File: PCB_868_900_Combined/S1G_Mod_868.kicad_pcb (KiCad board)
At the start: 4 copper layers, 60 x 27 mm, 82 parts, among them J2 20021121-00010C4LF, J5 0475890001-MicroUSBPort, P1 61301621121, Q1 DMG2307L-7, SW1 CUS-12TB, SW2 B3U-1000P, T1 0732511150, U1 AP7361-33FGE-7, U2 ADF7023BCPZ, U3 STM32L052C8T6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

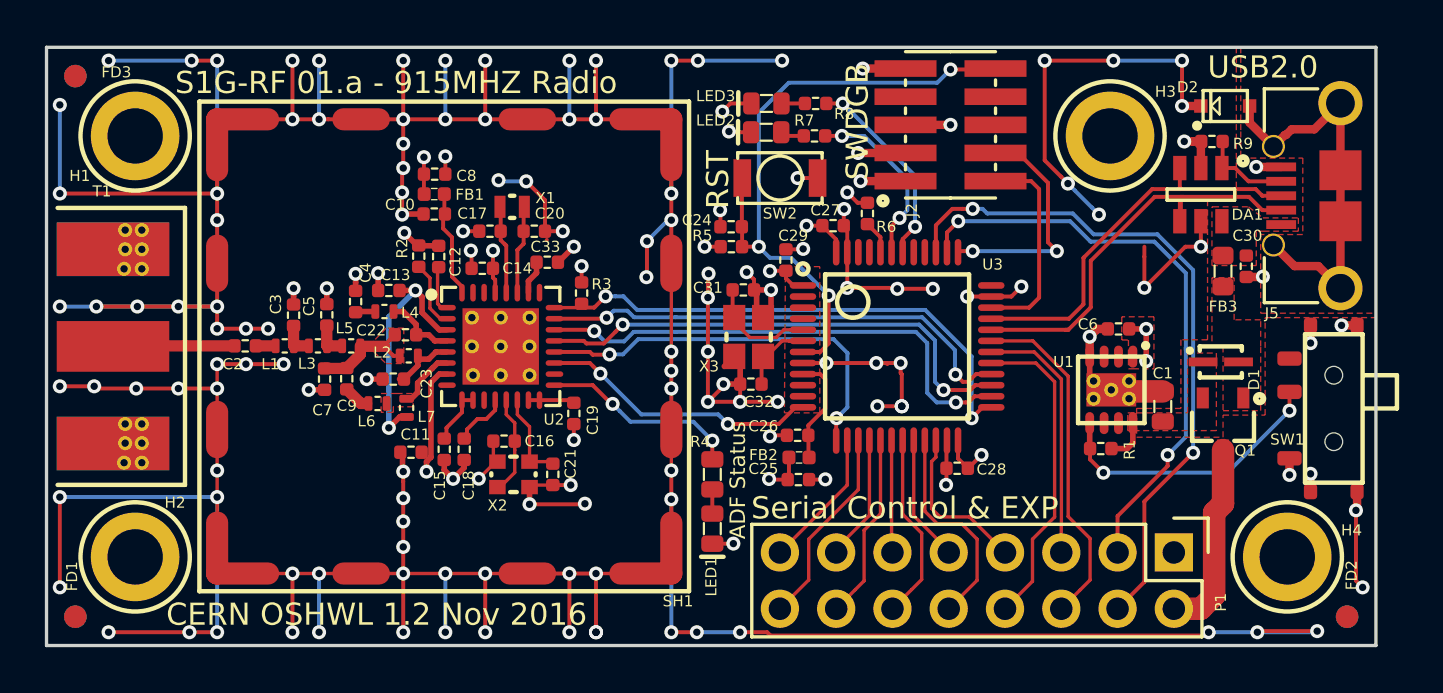
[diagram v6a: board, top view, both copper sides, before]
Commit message: LDO and Pwr LEd
Power LED added to combined radio and LDO section revamped.
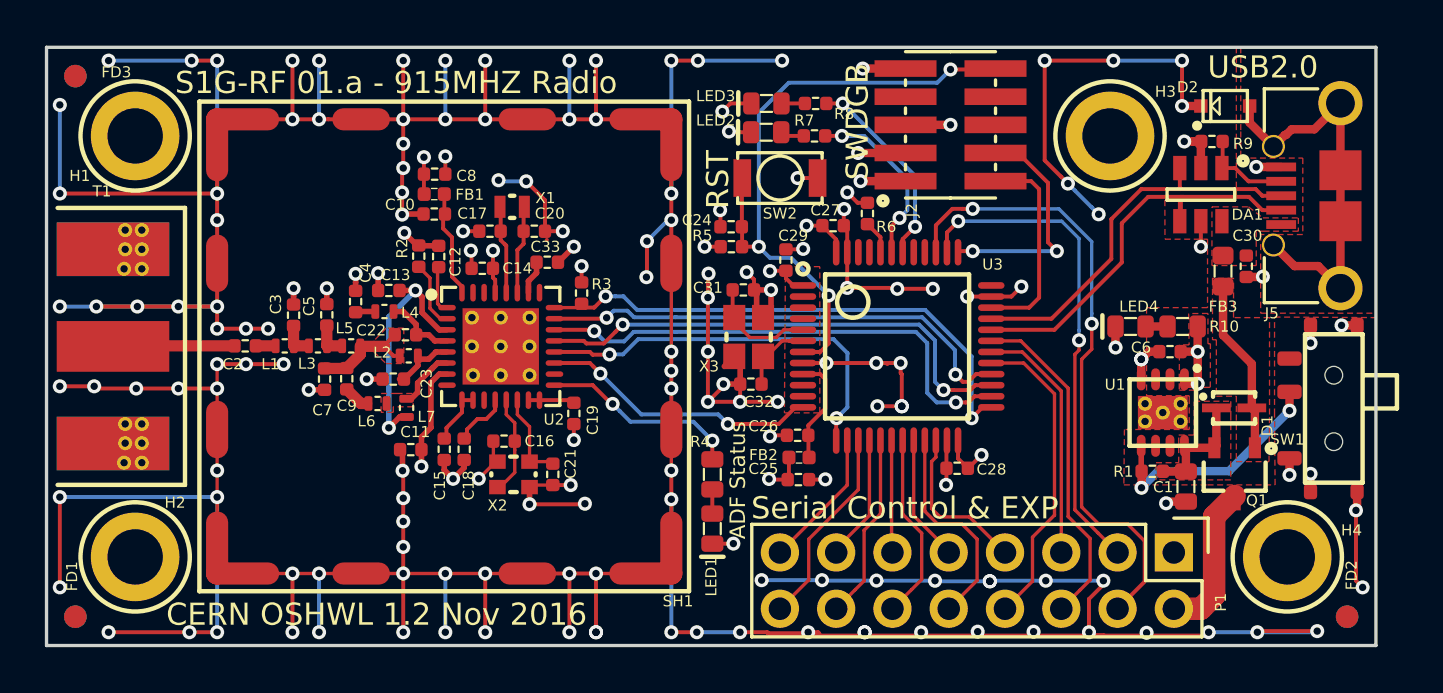
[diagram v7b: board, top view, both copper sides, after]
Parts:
- added LED4: LTST-C193KRKT-5A, PCB_Footprints:LED0603, F.Cu at (105.4, 50.6)
- added R10: RC1608J202CS, PCB_Footprints:R0603, F.Cu at (107.8, 50.6)
- moved C1 3.76 mm to (107.9, 57.8), turned to 270 degrees
- moved C6 2.54 mm to (107.2, 51.7)
- moved R1 2.54 mm to (106.4, 57.1)
- moved U1 2.54 mm to (106.9, 54.5)
- moved Q1 2.31 mm to (110.1, 57.2)
- moved D1 2.16 mm to (110.1, 54.3)
- moved C11 0.12 mm to (72.9, 56.2)
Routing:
- net GND: track 359.6 -> 373.3 mm, vias 157 -> 175
- net /VBUS: track 0.00 -> 7.87 mm
- net /MCU - STM32L052K8T6/GPIO_PA15: track 26.8 -> 22.4 mm
- net /VIN: track 1.97 -> 5.45 mm
- net /MCU - STM32L052K8T6/GPIO_PB3: track 31.0 -> 28.4 mm
- net /ON_OFF: track 12.9 -> 10.8 mm
- net /PSU_IN: track 8.80 -> 6.94 mm
- net +3V3: track 22.7 -> 24.3 mm
- net Net-(LED4-Pad1): track 0.00 -> 0.73 mm

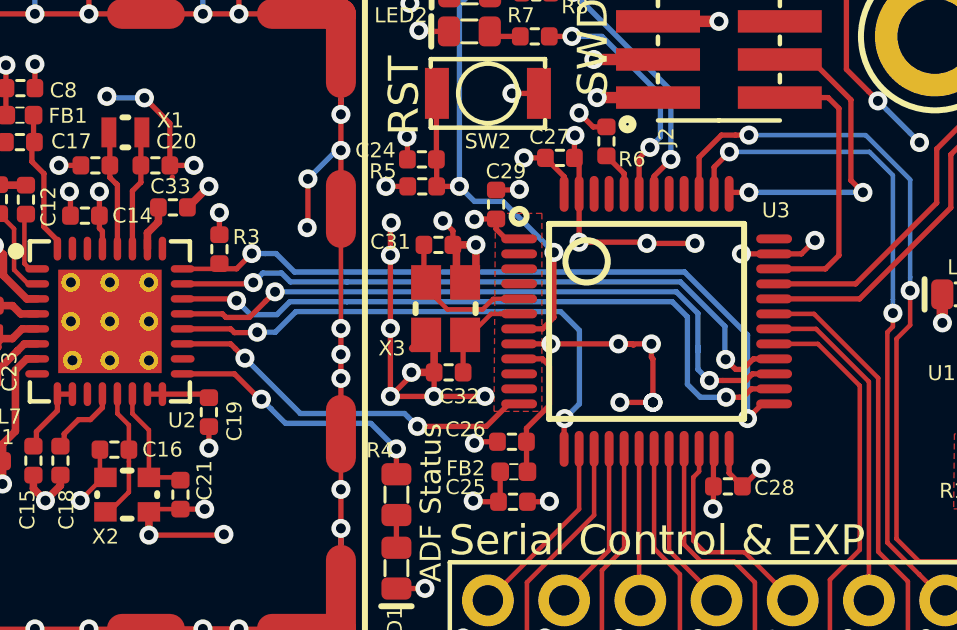
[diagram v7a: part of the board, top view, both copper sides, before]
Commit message: SPI Resistors
SPI resistors added to combined antenna implementation.
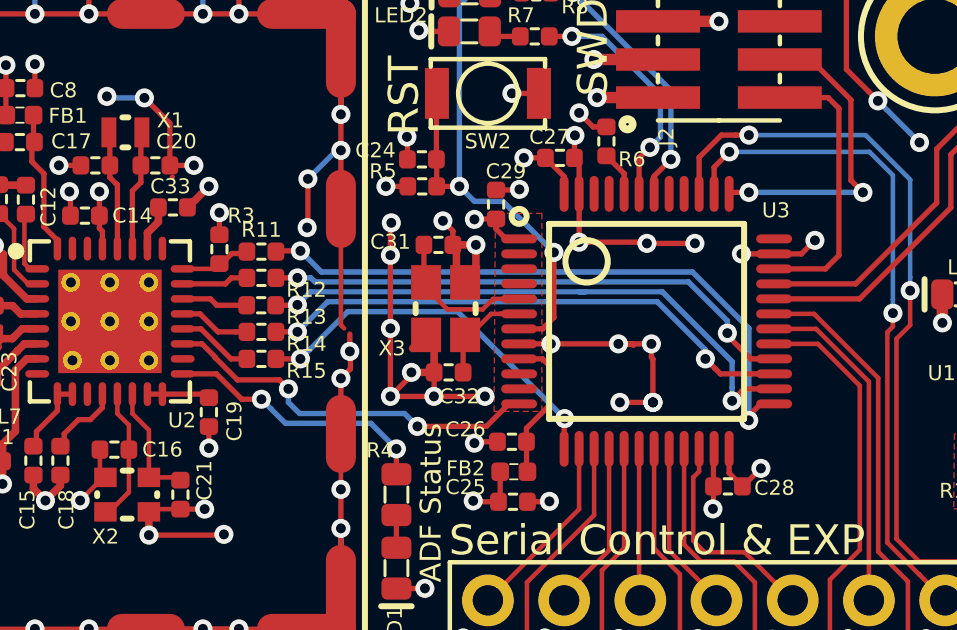
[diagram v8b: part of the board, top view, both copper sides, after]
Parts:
- added R11: TNPW0402100RBEED, PCB_Footprints:R0402, F.Cu at (82.0, 49.2)
- added R12: TNPW0402100RBEED, PCB_Footprints:R0402, F.Cu at (82.0, 50.0)
- added R13: TNPW0402100RBEED, PCB_Footprints:R0402, F.Cu at (82.0, 51.0)
- added R14: TNPW0402100RBEED, PCB_Footprints:R0402, F.Cu at (82.0, 51.9)
- added R15: TNPW0402100RBEED, PCB_Footprints:R0402, F.Cu at (82.0, 52.8)
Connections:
- R3 pad 2: /SPI_CS -> Net-(R11-Pad1)
- U2 pad 20: /MCU_IRQ -> Net-(R15-Pad1)
- U2 pad 21: /SPI_MISO -> Net-(R14-Pad1)
- U2 pad 22: /SPI_SCLK -> Net-(R13-Pad1)
- U2 pad 23: /SPI_MOSI -> Net-(R12-Pad1)
- U2 pad 24: /SPI_CS -> Net-(R11-Pad1)
- U3 pad 13: /MCU_IRQ -> /MCU - STM32L052K8T6/MCU_IRQ
- U3 pad 25: /SPI_CS -> /MCU - STM32L052K8T6/SPI_CS
- U3 pad 26: /SPI_SCLK -> /MCU - STM32L052K8T6/SPI_SCLK
- U3 pad 27: /SPI_MISO -> /MCU - STM32L052K8T6/SPI_MISO
- U3 pad 28: /SPI_MOSI -> /MCU - STM32L052K8T6/SPI_MOSI
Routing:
- net /SPI_CS: track 24.2 -> 0.00 mm, vias 2 -> 0
- net /SPI_SCLK: track 22.9 -> 0.00 mm, vias 2 -> 0
- net /SPI_MISO: track 22.7 -> 0.00 mm, vias 2 -> 0
- net /SPI_MOSI: track 22.0 -> 0.00 mm, vias 2 -> 0
- net /MCU - STM32L052K8T6/SPI_CS: track 0.00 -> 21.1 mm, vias 0 -> 2
- net /MCU - STM32L052K8T6/SPI_SCLK: track 0.00 -> 19.4 mm, vias 0 -> 2
- net /MCU - STM32L052K8T6/SPI_MISO: track 0.00 -> 18.2 mm, vias 0 -> 2
- net /MCU - STM32L052K8T6/SPI_MOSI: track 0.00 -> 18.0 mm, vias 0 -> 2
- net /MCU_IRQ: track 18.0 -> 0.00 mm, vias 2 -> 0
- net /MCU - STM32L052K8T6/MCU_IRQ: track 0.00 -> 12.8 mm, vias 0 -> 2
- net Net-(R11-Pad1): track 0.00 -> 2.82 mm
- net Net-(R15-Pad1): track 0.00 -> 2.56 mm
- net Net-(R14-Pad1): track 0.00 -> 2.39 mm
- net Net-(R12-Pad1): track 0.00 -> 2.22 mm
- net Net-(R13-Pad1): track 0.00 -> 2.22 mm
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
